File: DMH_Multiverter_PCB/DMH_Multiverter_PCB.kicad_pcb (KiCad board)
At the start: 2 copper layers, 32 x 75 mm, 22 parts, among them J0 Conn_01x01, J100 IDC_02x05, J200 BackBone_Connector_6pin, J50 Conn_01x06, J60 Conn_01x06, U1 TL072

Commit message: Created Gerbers
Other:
- board text added: "Mk1.0 - December 2024"
- board text removed: "Mk1.0 - Month Year"
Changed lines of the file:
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@@
 			(plot_on_all_layers_selection 0x0000000_00000000)
 			(disableapertmacros no)
-			(usegerberextensions no)
+			(usegerberextensions yes)
 			(usegerberattributes yes)
 			(usegerberadvancedattributes yes)
@@
 			(plotinvisibletext no)
 			(sketchpadsonfab no)
-			(subtractmaskfromsilk no)
+			(subtractmaskfromsilk yes)
 			(outputformat 1)
 			(mirror no)
-			(drillshape 1)
+			(drillshape 0)
 			(scaleselection 1)
-			(outputdirectory "")
+			(outputdirectory "Gerbers/")
 		)
 	)
@@
 		(layer "User.9")
 	)
-	(gr_text "Mk1.0 - Month Year"
-		(at 68.5 99 -90)
+	(gr_text "Mk1.0 - December 2024"
+		(at 68.5 99 270)
 		(layer "B.SilkS")
 		(effects

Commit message: Re-routing ongoing
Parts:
- removed R1, R4: 100k, Resistor_THT:R_Axial_DIN0207_L6.3mm_D2.5mm_P7.62mm_Horizontal
- added R7: 100k, Resistor_THT:R_Axial_DIN0207_L6.3mm_D2.5mm_P7.62mm_Horizontal, B.Cu at (72.5, 114.8)
- added R8: 82k, Resistor_THT:R_Axial_DIN0207_L6.3mm_D2.5mm_P7.62mm_Horizontal, B.Cu at (69.2, 107.2)
- added RV3: 50k, Potentiometer_THT:Potentiometer_Bourns_3296W_Vertical, B.Cu at (89.2, 73.7)
- added RV4: 50k, Potentiometer_THT:Potentiometer_Bourns_3296W_Vertical, B.Cu at (89.2, 84.0)
- R2, R5: value 100k -> 33k
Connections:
- J200 pad 3: Net-(J200-Pin_3) -> GND
- J200 pad 4: Net-(J200-Pin_4) -> Net-(J200-Pin_1)
- J200 pad 5: GND -> Net-(J200-Pin_2)
- J60 pad 1: Net-(J200-Pin_1) -> Net-(J60-Pin_1)
- J60 pad 2: Net-(J200-Pin_2) -> Net-(J200-Pin_1)
- J60 pad 3: Net-(J200-Pin_3) -> Net-(J60-Pin_1)
- J60 pad 4: Net-(J200-Pin_4) -> Net-(J200-Pin_2)
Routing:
- net /Core Circuit/Att B Input: track 53.9 -> 16.6 mm
- net /Core Circuit/Att B Output: track 35.6 -> 0.00 mm
- net +12V: track 30.5 -> 63.2 mm
- net /Core Circuit/Att A Output: track 30.9 -> 0.00 mm
- net Net-(U1B--): track 25.1 -> 0.00 mm
- net Net-(J60-Pin_1): track 0.00 -> 22.7 mm
- net Net-(J200-Pin_4): track 21.3 -> 0.00 mm
- net Net-(R5-Pad2): track 23.7 -> 3.25 mm
- net Net-(J200-Pin_3): track 17.3 -> 0.00 mm
- net Net-(R2-Pad2): track 15.9 -> 3.25 mm
- net Net-(U1A--): track 10.5 -> 0.00 mm
- net /Core Circuit/Att A Input: track 23.4 -> 15.9 mm
- net Net-(J200-Pin_2): track 13.7 -> 18.3 mm
- net Net-(J200-Pin_1): track 10.1 -> 13.7 mm
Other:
- board text added: "Mk2.0 - December 2024"
- board text removed: "Mk1.0 - December 2024"

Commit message: Finished routing Mk2 version
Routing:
- net /Core Circuit/Att B Output: track 0.00 -> 35.5 mm
- net /Core Circuit/Att B Input: track 16.6 -> 49.6 mm
- net /Core Circuit/Att A Output: track 0.00 -> 30.8 mm
- net Net-(U1B--): track 0.00 -> 24.0 mm
- net Net-(R5-Pad2): track 3.25 -> 23.7 mm
- net Net-(R2-Pad2): track 3.25 -> 17.4 mm
- net Net-(U1A--): track 0.00 -> 12.9 mm
- net /Core Circuit/Att A Input: track 15.9 -> 22.5 mm
- net Net-(J200-Pin_2): track 18.3 -> 19.3 mm

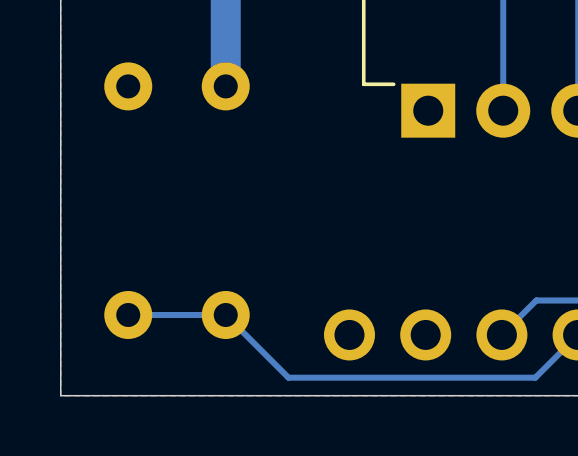
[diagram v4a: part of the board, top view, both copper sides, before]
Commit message: Finished Mk2 design
- Changed R7 value to 10k
- Replaced the other resistor with a 5V1 Zener
- Cleaned up schematic
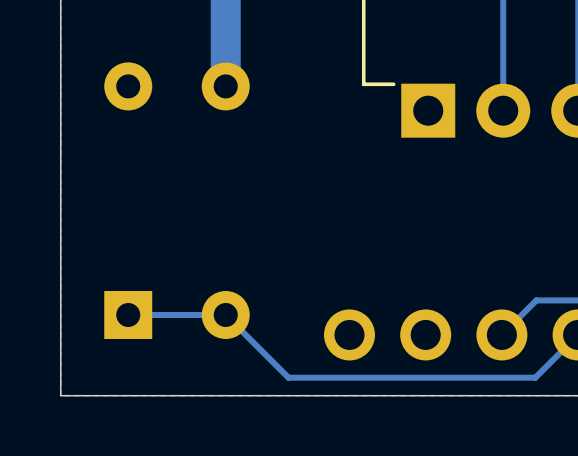
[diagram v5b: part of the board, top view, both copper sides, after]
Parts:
- removed R8: 82k, Resistor_THT:R_Axial_DIN0207_L6.3mm_D2.5mm_P7.62mm_Horizontal
- added D3: 5V1, Diode_THT:D_DO-35_SOD27_P7.62mm_Horizontal, B.Cu at (69.2, 114.8)
- R7: value 100k -> 10k

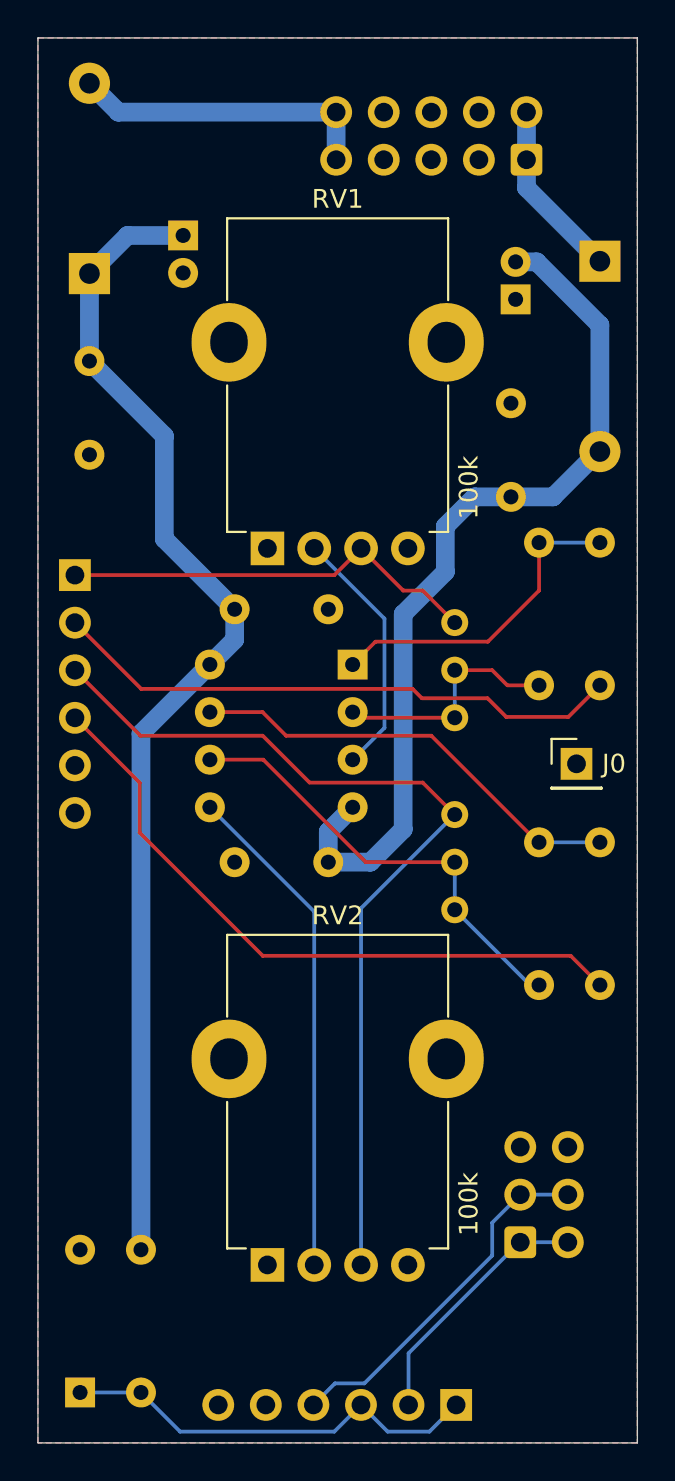
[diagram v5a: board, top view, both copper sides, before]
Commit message: Switched adjustment trimpots position with Rin
... and renumbered the resistors.
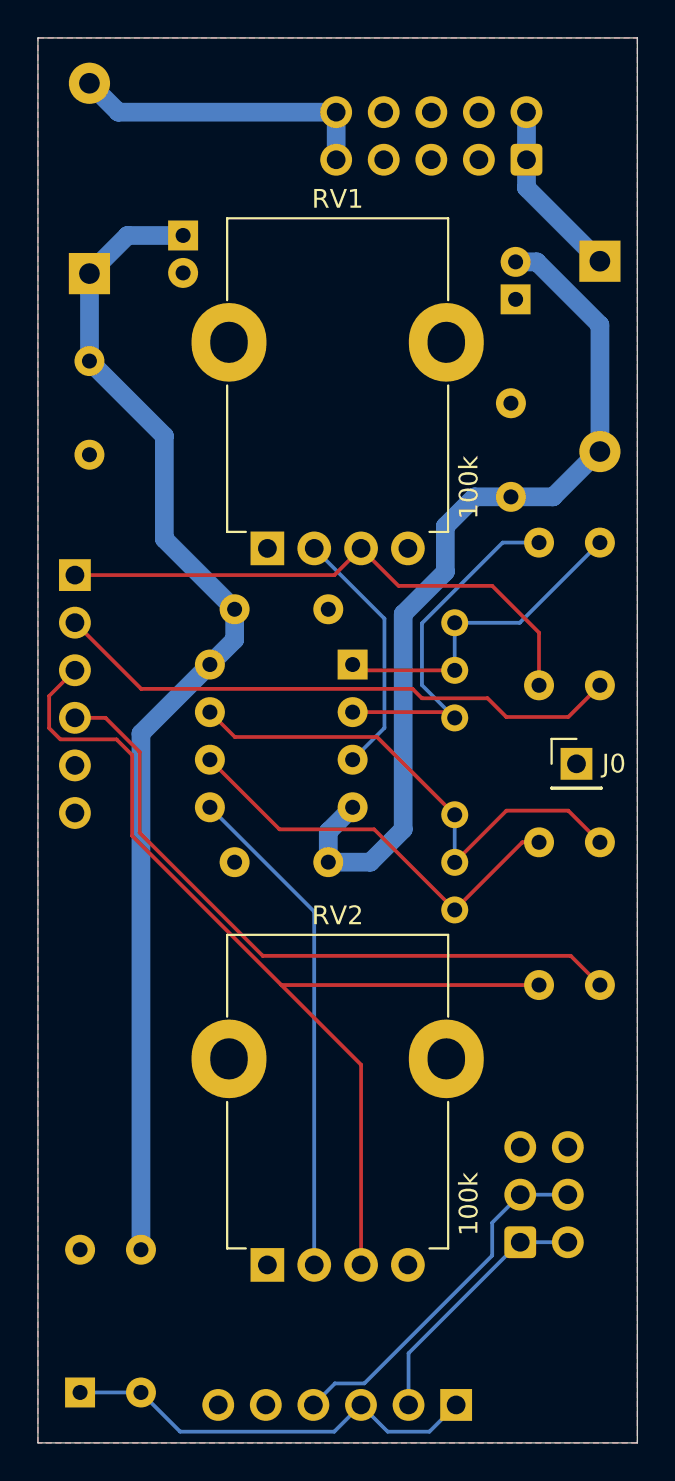
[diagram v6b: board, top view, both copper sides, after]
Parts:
- D3: value 5V1 -> ZPD5V1
- moved RV3 5.09 mm to (89.2, 78.8), turned to -90 degrees
- moved RV4 5.09 mm to (89.2, 89.0), turned to -90 degrees
- renumbered R2 to R1, R3 to R2, R5 to R3, R6 to R4, R7 to R5
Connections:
- R1 pad 1: Net-(U1A--) -> /Core Circuit/Att A Input
- R1 pad 2: Net-(R2-Pad2) -> Net-(U1A--)
- R2 pad 1: Net-(R2-Pad2) -> Net-(R2-Pad1)
- R3 pad 1: Net-(U1B--) -> /Core Circuit/Att B Input
- R3 pad 2: Net-(R5-Pad2) -> Net-(U1B--)
- R4 pad 1: Net-(R5-Pad2) -> Net-(R4-Pad1)
- RV3 pad 1: /Core Circuit/Att A Input -> Net-(U1A--)
- RV3 pad 2: Net-(U1A--) -> Net-(R2-Pad1)
- RV3 pad 3: Net-(U1A--) -> Net-(R2-Pad1)
- RV4 pad 1: /Core Circuit/Att B Input -> Net-(U1B--)
- RV4 pad 2: Net-(U1B--) -> Net-(R4-Pad1)
- RV4 pad 3: Net-(U1B--) -> Net-(R4-Pad1)
- U1 pad 1: Net-(R2-Pad2) -> Net-(R2-Pad1)
- U1 pad 7: Net-(R5-Pad2) -> Net-(R4-Pad1)
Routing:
- net Net-(R4-Pad1): track 0.00 -> 27.5 mm
- net Net-(R5-Pad2): track 23.7 -> 0.00 mm
- net Net-(R2-Pad1): track 0.00 -> 17.6 mm
- net Net-(R2-Pad2): track 17.4 -> 0.00 mm
- net /Core Circuit/Att A Input: track 22.5 -> 30.0 mm
- net Net-(U1A--): track 12.9 -> 19.8 mm
- net /Core Circuit/Att B Input: track 49.6 -> 54.7 mm
- net Net-(U1B--): track 24.0 -> 22.4 mm
- net /Core Circuit/Att B Output: track 35.5 -> 36.5 mm

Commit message: Generated PCB Mk1.5 Gerbers
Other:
- board text added: "Mk1.5 - March 2025"
- board text removed: "Mk2.0 - December 2024"
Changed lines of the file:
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@@
 		(layer "B.Cu")
 		(at 83.8 75.95 180)
-		(descr "8-lead though-hole mounted DIP package, row spacing 7.62 mm (300 mils), Socket")
+		(descr "8-lead though-hole mounted DIP package, row spacing 7.62mm (300 mils), Socket")
 		(tags "THT DIP DIL PDIP 2.54mm 7.62mm 300mil Socket")
 		(property "Reference" "U1"
@@
 		(attr through_hole)
 		(fp_line
-			(start 8.95 1.39)
-			(end 8.95 -9.01)
-			(stroke
-				(width 0.12)
-				(type solid)
-			)
-			(layer "B.SilkS")
-		)
-		(fp_line
-			(start 8.95 -9.01)
-			(end -1.33 -9.01)
-			(stroke
-				(width 0.12)
-				(type solid)
-			)
-			(layer "B.SilkS")
-		)
-		(fp_line
 			(start 6.46 1.33)
-			(end 6.46 -8.95)
+			(end 4.81 1.33)
 			(stroke
 				(width 0.12)
@@
 		(fp_line
 			(start 6.46 -8.95)
-			(end 1.16 -8.95)
+			(end 6.46 1.33)
 			(stroke
 				(width 0.12)
@@
 		)
 		(fp_line
-			(start 4.81 1.33)
-			(end 6.46 1.33)
+			(start 2.81 1.33)
+			(end 1.16 1.33)
 			(stroke
 				(width 0.12)
@@
 		(fp_line
 			(start 1.16 1.33)
-			(end 2.81 1.33)
+			(end 1.16 -8.95)
 			(stroke
 				(width 0.12)
@@
 		(fp_line
 			(start 1.16 -8.95)
-			(end 1.16 1.33)
+			(end 6.46 -8.95)
 			(stroke
 				(width 0.12)
@@
 			(layer "B.SilkS")
 		)
-		(fp_line
+		(fp_rect
 			(start -1.33 1.39)
-			(end 8.95 1.39)
-			(stroke
-				(width 0.12)
-				(type solid)
-			)
-			(layer "B.SilkS")
-		)
-		(fp_line
-			(start -1.33 -9.01)
-			(end -1.33 1.39)
+			(end 8.95 -9.01)
 			(stroke
 				(width 0.12)
 				(type solid)
 			)
+			(fill no)
 			(layer "B.SilkS")
 		)
@@
 			(layer "B.SilkS")
 		)
-		(fp_line
-			(start 9.15 1.6)
-			(end 9.15 -9.2)
-			(stroke
-				(width 0.05)
-				(type solid)
-			)
-			(layer "B.CrtYd")
-		)
-		(fp_line
-			(start 9.15 -9.2)
-			(end -1.55 -9.2)
-			(stroke
-				(width 0.05)
-				(type solid)
-			)
-			(layer "B.CrtYd")
-		)
-		(fp_line
-			(start -1.55 1.6)
-			(end 9.15 1.6)
-			(stroke
-				(width 0.05)
-				(type solid)
-			)
-			(layer "B.CrtYd")
-		)
-		(fp_line
-			(start -1.55 -9.2)
-			(end -1.55 1.6)
+		(fp_rect
+			(start -1.52 1.58)
+			(end 9.14 -9.2)
 			(stroke
 				(width 0.05)
 				(type solid)
 			)
+			(fill no)
 			(layer "B.CrtYd")
 		)
 		(fp_line
-			(start 8.89 1.33)
-			(end 8.89 -8.95)
-			(stroke
-				(width 0.1)
-				(type solid)
-			)
-			(layer "B.Fab")
-		)
-		(fp_line
-			(start 8.89 -8.95)
-			(end -1.27 -8.95)
-			(stroke
-				(width 0.1)
-				(type solid)
-			)
-			(layer "B.Fab")
-		)
-		(fp_line
 			(start 6.985 1.27)
-			(end 1.635 1.27)
+			(end 6.985 -8.89)
 			(stroke
 				(width 0.1)
@@
 		(fp_line
 			(start 6.985 -8.89)
-			(end 6.985 1.27)
+			(end 0.635 -8.89)
 			(stroke
 				(width 0.1)
@@
 		(fp_line
 			(start 1.635 1.27)
-			(end 0.635 0.27)
+			(end 6.985 1.27)
 			(stroke
 				(width 0.1)
@@
 		(fp_line
 			(start 0.635 0.27)
-			(end 0.635 -8.89)
+			(end 1.635 1.27)
 			(stroke
 				(width 0.1)
@@
 		(fp_line
 			(start 0.635 -8.89)
-			(end 6.985 -8.89)
+			(end 0.635 0.27)
 			(stroke
 				(width 0.1)
@@
 			(layer "B.Fab")
 		)
-		(fp_line
+		(fp_rect
 			(start -1.27 1.33)
-			(end 8.89 1.33)
-			(stroke
-				(width 0.1)
-				(type solid)
-			)
-			(layer "B.Fab")
-		)
-		(fp_line
-			(start -1.27 -8.95)
-			(end -1.27 1.33)
+			(end 8.89 -8.95)
 			(stroke
 				(width 0.1)
 				(type solid)
 			)
+			(fill no)
 			(layer "B.Fab")
 		)
@@
 			)
 		)
-		(pad "1" thru_hole rect
+		(pad "1" thru_hole roundrect
 			(at 0 0 180)
 			(size 1.6 1.6)
@@
 			(layers "*.Cu" "*.Mask")
 			(remove_unused_layers no)
+			(roundrect_rratio 0.15625)
 			(net 13 "Net-(R2-Pad1)")
 			(pintype "output")
 		)
-		(pad "2" thru_hole oval
+		(pad "2" thru_hole circle
 			(at 0 -2.54 180)
 			(size 1.6 1.6)
@@
 			(pintype "input")
 		)
-		(pad "3" thru_hole oval
+		(pad "3" thru_hole circle
 			(at 0 -5.08 180)
 			(size 1.6 1.6)
@@
 			(pintype "input")
 		)
-		(pad "4" thru_hole oval
+		(pad "4" thru_hole circle
 			(at 0 -7.62 180)
 			(size 1.6 1.6)
@@
 			(pintype "power_in")
 		)
-		(pad "5" thru_hole oval
+		(pad "5" thru_hole circle
 			(at 7.62 -7.62 180)
 			(size 1.6 1.6)
@@
 			(pintype "input")
 		)
-		(pad "6" thru_hole oval
+		(pad "6" thru_hole circle
 			(at 7.62 -5.08 180)
 			(size 1.6 1.6)
@@
 			(pintype "input")
 		)
-		(pad "7" thru_hole oval
+		(pad "7" thru_hole circle
 			(at 7.62 -2.54 180)
 			(size 1.6 1.6)
@@
 			(pintype "output")
 		)
-		(pad "8" thru_hole oval
+		(pad "8" thru_hole circle
 			(at 7.62 0 180)
 			(size 1.6 1.6)
@@
 		)
 		(embedded_fonts no)
-		(model "${KICAD8_3DMODEL_DIR}/Package_DIP.3dshapes/DIP-8_W7.62mm_Socket.wrl"
+		(model "${KICAD9_3DMODEL_DIR}/Package_DIP.3dshapes/DIP-8_W7.62mm_Socket.wrl"
 			(offset
 				(xyz 0 0 0)
@@
 			(at 5.08 -2.47 90)
 			(layer "B.Fab")
+			(hide yes)
 			(effects
 				(font
@@
 			(at 0 -15.47 90)
 			(layer "B.Fab")
+			(hide yes)
 			(effects
 				(font
@@
 			(at 0 -15.47 0)
 			(layer "B.Fab")
+			(hide yes)
 			(effects
 				(font
@@
 			(at 1.27 -11.18 0)
 			(layer "B.Fab")
+			(hide yes)
 			(effects
 				(font
@@
 		(layer "User.9")
 	)
-	(gr_text "Mk2.0 - December 2024"
+	(gr_text "Mk1.5 - March 2025"
 		(at 68.5 96 270)
 		(layer "B.SilkS")
